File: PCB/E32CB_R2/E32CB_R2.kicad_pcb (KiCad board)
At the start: 2 copper layers, 111.3 x 90.9 mm, 89 parts, among them J1 GPIO_HEADER, J10 S, J11 Q4, J12 S, J13 Q3, J14 S, J15 Q8, J16 S, J17 Q7, J18 S, J19 Q6, J2 Power, J20 S, J21 Q5, J22 S, J3 USB_B, J4 USB +5V, J5 NEXTION, J6 I2C, J7 Q1, J8 S, J9 Q2, Q1 S8050, Q10 IRLR2905, Q2 S8050, Q3 IRLR2905, Q4 IRLR2905, Q5 IRLR2905, Q6 IRLR2905, Q7 IRLR2905, Q8 IRLR2905, Q9 IRLR2905, U1 ESP32-WROOM-32, X1 12MHz

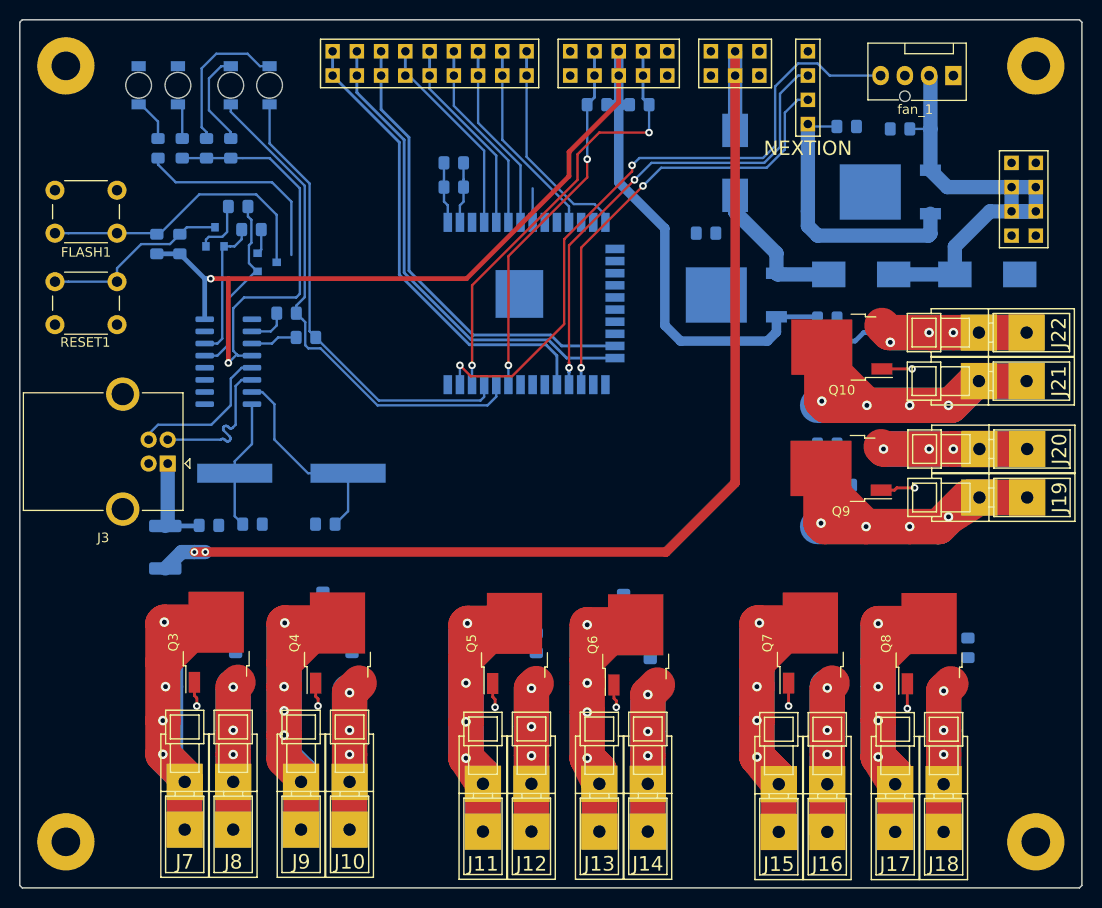
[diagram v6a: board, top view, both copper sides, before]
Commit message: mosfet connection
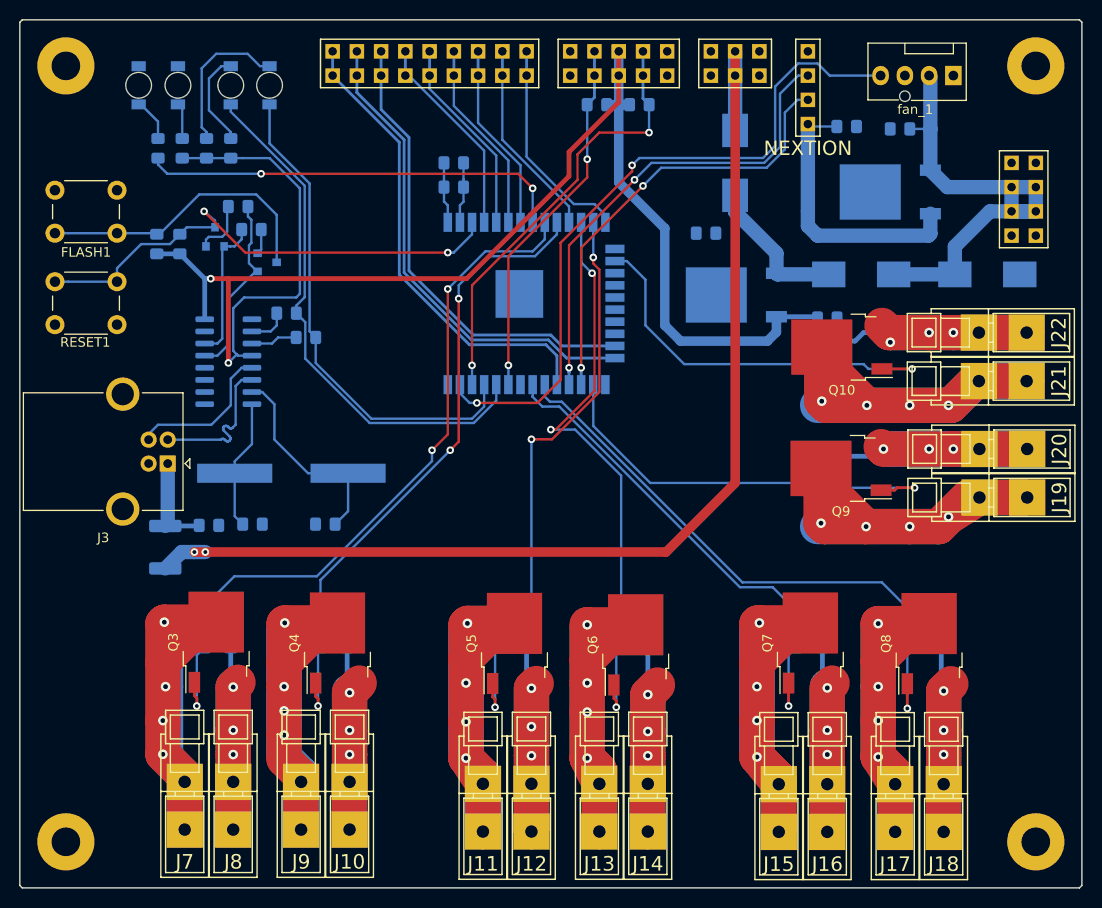
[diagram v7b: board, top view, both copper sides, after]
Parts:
- moved R14 3.81 mm to (128.3, 110.7)
- moved R18 3.57 mm to (159.8, 110.7)
- moved R21 3.06 mm to (178.1, 110.7)
- moved R26 2.97 mm to (193.3, 110.7)
- moved R13 2.17 mm to (116.1, 110.7)
- moved R23 1.55 mm to (181.4, 94.5)
- moved R27 1.27 mm to (181.4, 91.7)
- moved R20 1.16 mm to (162.6, 110.7)
- moved R19 1.14 mm to (149.9, 110.7)
- moved R22 1.02 mm to (190.5, 110.7)
- moved R16 0.71 mm to (131.1, 110.7)
- moved R15 0.71 mm to (118.9, 110.7)
- moved R25 0.51 mm to (180.8, 110.7)
- moved R17 0.26 mm to (147.1, 110.7)
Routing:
- net /Q1: track 0.00 -> 65.3 mm, vias 0 -> 2
- net /Q2: track 0.00 -> 55.7 mm, vias 0 -> 2
- net /Q7: track 0.00 -> 50.9 mm
- net /Q3: track 0.00 -> 49.8 mm, vias 0 -> 2
- net /Q4: track 0.00 -> 48.4 mm, vias 0 -> 2
- net /Q8: track 0.00 -> 40.0 mm
- net /EN: track 20.0 -> 54.2 mm, vias 0 -> 2
- net /Q6: track 0.00 -> 30.3 mm
- net /Q5: track 0.00 -> 28.5 mm
- net /s_LED: track 25.4 -> 44.5 mm, vias 0 -> 2
- net Net-(Q9-Pad1): track 3.61 -> 11.9 mm
- net Net-(Q10-Pad1): track 3.16 -> 11.2 mm
- net Net-(Q8-Pad1): track 2.60 -> 9.25 mm
- net Net-(Q5-Pad1): track 2.59 -> 9.01 mm
- net Net-(Q6-Pad1): track 2.44 -> 8.86 mm
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
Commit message: conection finished
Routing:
- net /IO_0: track 30.9 -> 83.7 mm, vias 0 -> 2
- net +3V3: track 176.0 -> 181.2 mm, vias 2 -> 3
- net /Q4: track 48.4 -> 48.9 mm
